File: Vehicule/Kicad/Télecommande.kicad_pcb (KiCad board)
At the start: 2 copper layers, 77.7 x 40 mm, 5 parts, among them J1 Conn_01x02_Socket, U1 ESP32-C3_SUPERMINI

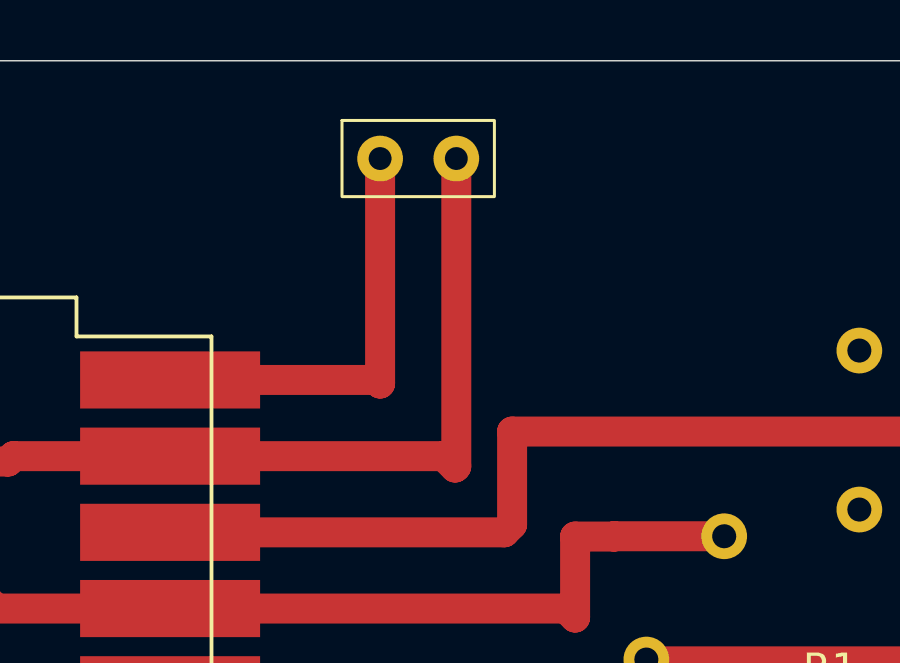
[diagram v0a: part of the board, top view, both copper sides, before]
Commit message: Suppression des anciennes versions du projet Télécommande
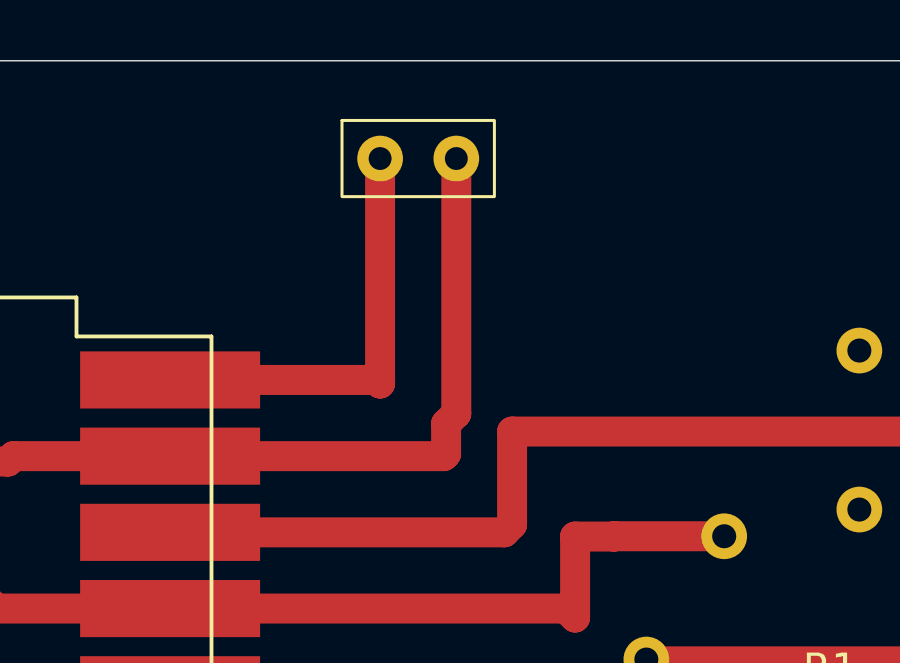
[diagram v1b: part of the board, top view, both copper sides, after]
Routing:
- net GND: track 73.5 -> 72.8 mm
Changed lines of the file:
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@@
+	)
+	(segment
+		(start 79.3 62.1)
+		(end 79.64 61.76)
+		(width 1)
+		(layer "F.Cu")
+		(net 23)
 	)
 	(segment
@@
 	)
 	(segment
-		(start 79.64 63.52)
-		(end 79.64 53.26)
-		(width 1)
-		(layer "F.Cu")
-		(net 23)
-	)
-	(segment
 		(start 93.06 79.12)
 		(end 93.675 79.735)
@@
 	)
 	(segment
+		(start 79.3 63.1)
+		(end 79.3 62.1)
+		(width 1)
+		(layer "F.Cu")
+		(net 23)
+	)
+	(segment
+		(start 79.64 61.76)
+		(end 79.64 53.26)
+		(width 1)
+		(layer "F.Cu")
+		(net 23)
+	)
+	(segment
 		(start 88.48 79.12)
 		(end 93.06 79.12)
+		(width 1)
+		(layer "F.Cu")
+		(net 23)
+	)
+	(segment
+		(start 70.1 63.18)
+		(end 79.22 63.18)
 		(width 1)
 		(layer "F.Cu")
@@
 	)
 	(segment
-		(start 79.22 63.18)
-		(end 79.6 63.56)
-		(width 1)
-		(layer "F.Cu")
-		(net 23)
-	)
-	(segment
-		(start 79.6 63.56)
-		(end 79.64 63.52)
-		(width 1)
-		(layer "F.Cu")
-		(net 23)
-	)
-	(segment
 		(start 83.6 65.86)
 		(end 84.9 65.86)
@@
 	)
 	(segment
-		(start 70.1 63.18)
-		(end 79.22 63.18)
+		(start 79.22 63.18)
+		(end 79.3 63.1)
 		(width 1)
 		(layer "F.Cu")
